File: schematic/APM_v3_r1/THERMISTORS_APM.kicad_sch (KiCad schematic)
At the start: 10 parts

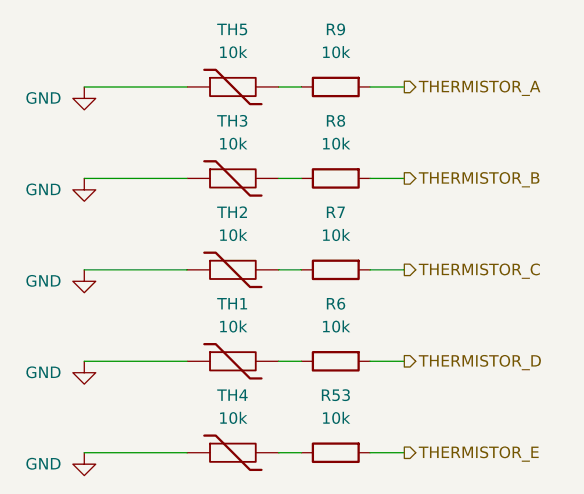
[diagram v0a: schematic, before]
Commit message: updating top v10. need to get 3v3 APM converged in schematic. routing is tricky right now. the components should be evenly laid out and have the NUCLEO pins be adjusted based on location
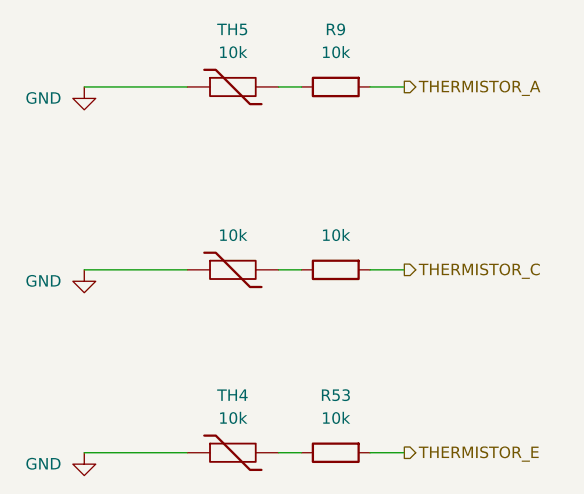
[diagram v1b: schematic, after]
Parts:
- removed R6, R8: 10k, Resistor_SMD:R_0805_2012Metric_Pad1.20x1.40mm_HandSolder, symbol Device:R
- removed TH1, TH3: 10k, Package_TO_SOT_THT:Heraeus_TO-92-2, symbol Device:Thermistor
- R53, R7, R9: footprint Resistor_SMD:R_0805_2012Metric_Pad1.20x1.40mm_HandSolder -> Resistor_SMD:R_0201_0603Metric
